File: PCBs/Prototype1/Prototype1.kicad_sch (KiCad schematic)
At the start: 152 parts, among them J2 CMOD-A7, J3 PMOD, J4 2x20_Conn, Q1 2N7002NXAK, Q10 2N7002NXAK, Q11 2N7002NXAK, Q12 2N7002NXAK, Q13 2N7002NXAK, Q14 2N7002NXAK, Q15 2N7002NXAK, Q16 2N7002NXAK, Q17 2N7002NXAK, Q18 2N7002NXAK, Q2 2N7002NXAK, Q3 2N7002NXAK, Q4 2N7002NXAK, Q5 2N7002NXAK, Q6 2N7002NXAK, Q7 2N7002NXAK, Q8 2N7002NXAK, Q9 2N7002NXAK, U1 FXMAR2104UMX, U10 FXMAR2104UMX, U11 74LVC3G14, U12 FXMAR2104UMX, U2 FXMAR2104UMX, U3 FXMAR2104UMX, U4 FXMAR2104UMX, U5 FXMAR2104UMX, U6 FXMAR2104UMX, U7 74LVC3G14, U8 FXMAR2104UMX, U9 74LVC3G14

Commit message: Made prototype board and completed more verilog conversions
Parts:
- added C23: .1uf, Capacitor_SMD:C_0402_1005Metric, symbol Device:C
- added C24: 10uf, Capacitor_SMD:C_0805_2012Metric, symbol Device:C
- added J1: Conn_01x03_Pin, Connector_PinSocket_2.54mm:PinSocket_1x03_P2.54mm_Vertical, symbol Connector:Conn_01x03_Pin
- added TP91, TP92, TP93, TP94, TP95, TP96, TP97, TP98: ~, POKEY_Footprints:TP, symbol Connector:TestPoint_Small
- added U13: LD1117S33TR, POKEY_Footprints:Reg, symbol Regulator_Linear:LD1117S33TR_SOT223
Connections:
- net +3.3V: now also J1.2 (Pin_2); no longer J3.12 (V), J3.6 (V)
- net +5V: now also C23.1, U13.3 (VI)
- net GND: now also C23.2, C24.2, U13.1 (GND)
- net OE: now also TP98.1
- net _DUMP: now also TP97.1
- net at J3.10 (JA10): now also TP91.1
- net at J3.2 (JA2): now also TP94.1
- net at J3.3 (JA3): now also TP95.1
- net at J3.4 (JA4): now also TP96.1
- net at J3.8 (JA8): now also TP93.1
- net at J3.9 (JA9): now also TP92.1
- new net 3V3_A: J1.1 (Pin_1), J3.12 (V), J3.6 (V)
- new net 3V3_B: C24.1, J1.3 (Pin_3), U13.2 (VO)
- no-connect marks 12 -> 6
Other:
- note added: "Arcade PCB Interface"
- note removed: "Arcade PCB Interface and Optional POKEY Slot"
- note removed: "POKEY Socket (Optional)"
- moved on the sheet: J4, TP1, TP10, TP11, TP12, TP13, TP14, TP15, TP16, TP17, TP18, TP19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

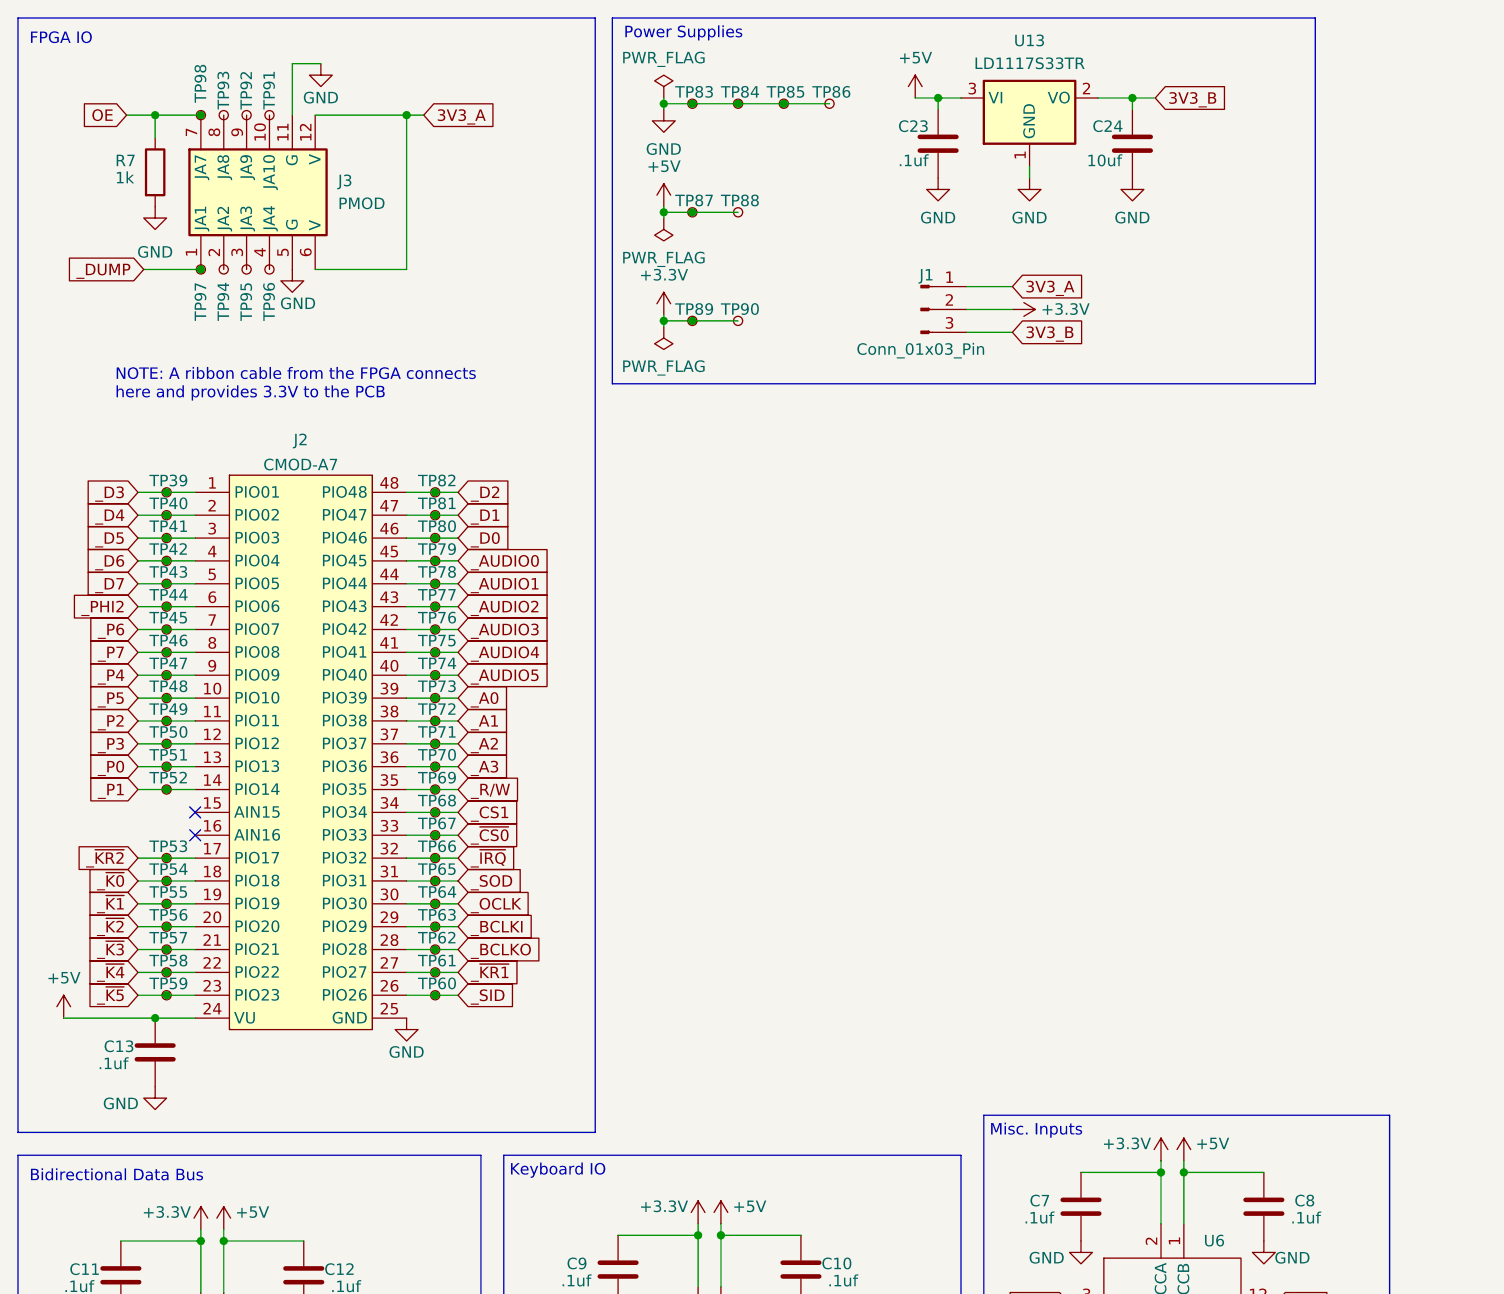
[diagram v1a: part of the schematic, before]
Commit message: Finished verilog POKEY code
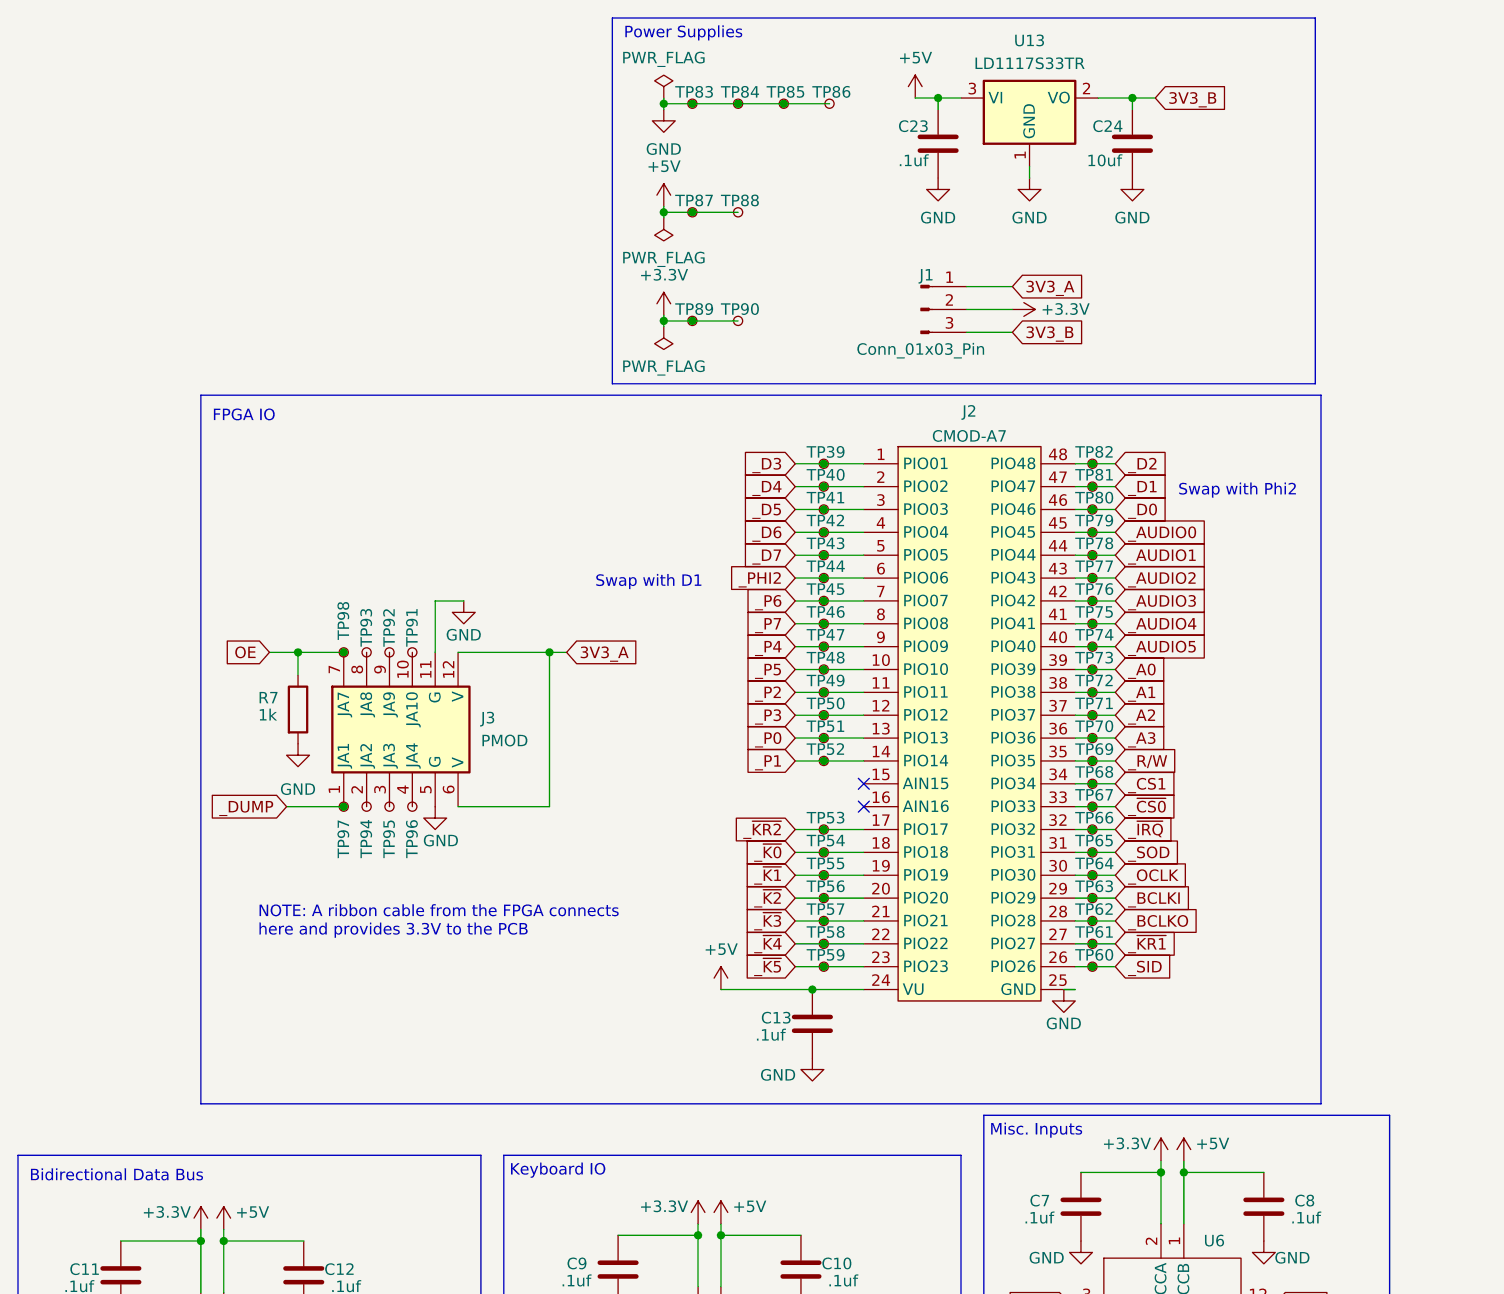
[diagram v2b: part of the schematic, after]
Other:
- note added: "Swap with D1"
- note added: "Swap with Phi2"
- moved on the sheet: C13, J2, J3, R7, TP39, TP40, TP41, TP42, TP43, TP44, TP45, TP46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

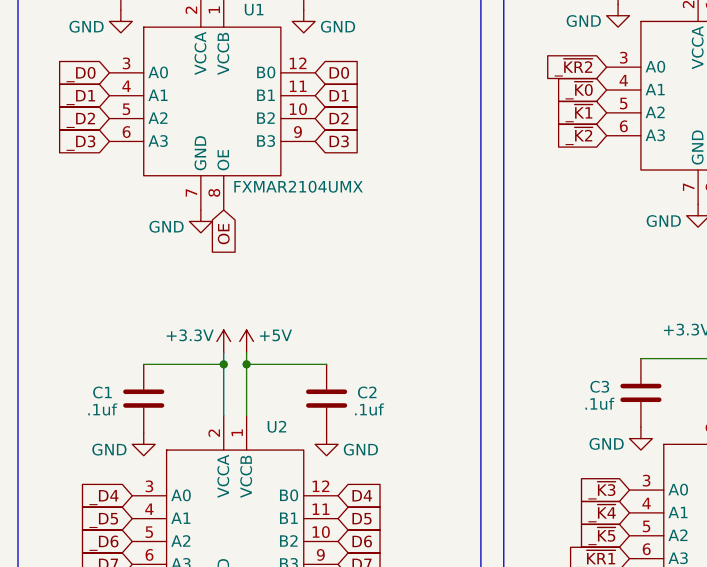
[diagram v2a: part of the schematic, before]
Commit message: Added new prototype PCBs
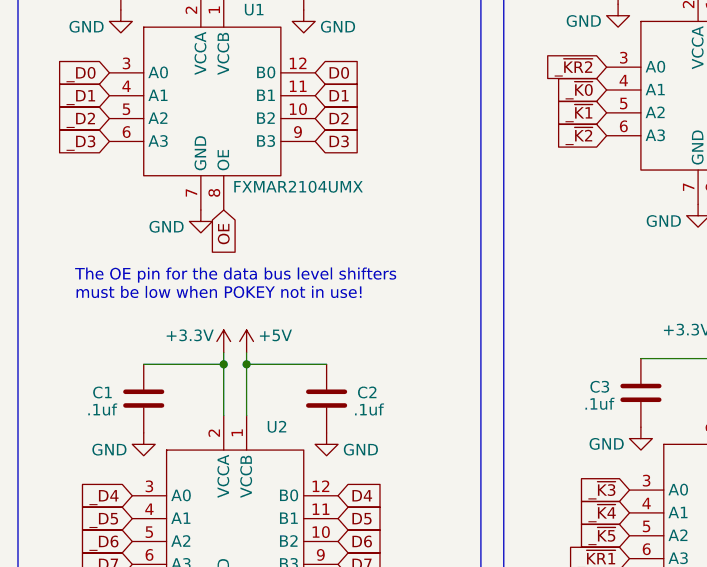
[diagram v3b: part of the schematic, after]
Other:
- note added: "The OE pin for the data bus level shifters must be low when POKEY not in use!"
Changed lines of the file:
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@@
+    (effects (font (size 1.27 1.27)) (justify left bottom))
+  )
+  (text "The OE pin for the data bus level shifters \nmust be low when POKEY not in use!"
+    (at 23.495 196.215 0)
     (effects (font (size 1.27 1.27)) (justify left bottom))
   )
